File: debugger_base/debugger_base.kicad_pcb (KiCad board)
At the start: 4 copper layers, 57.4 x 50.8 mm, 62 parts, among them SW1 RESET, SW2 UART CHx LED enable switch, X1 USB-C Receptacle, X2 Channel A, X3 Channel B, X4 Channel C, X5 Channel D, Y1 12MHz

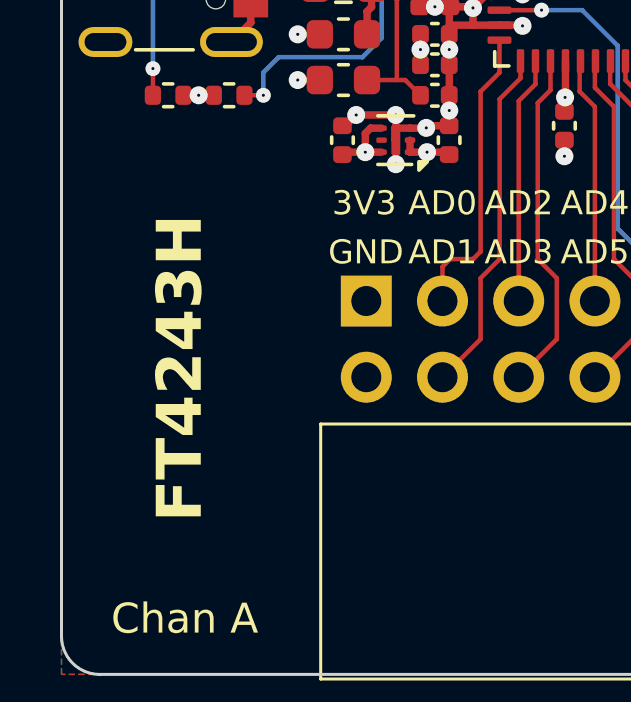
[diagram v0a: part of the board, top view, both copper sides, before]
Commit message: add version number to silkscreen
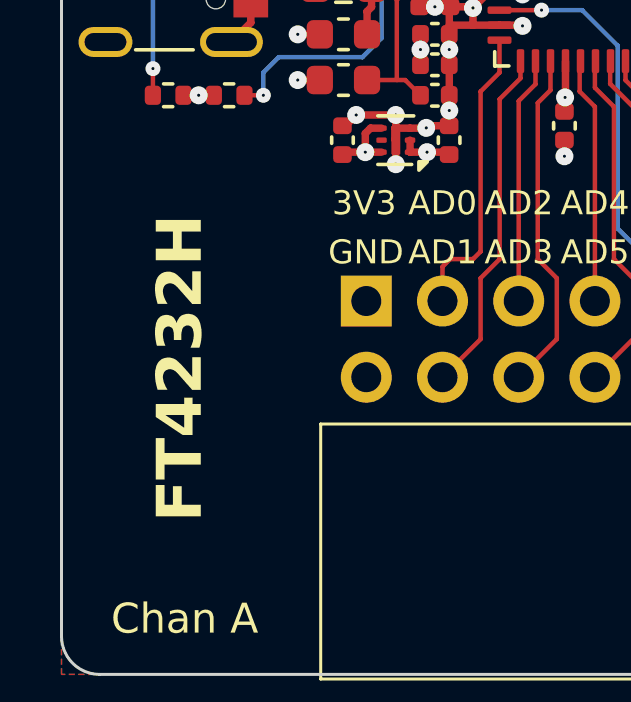
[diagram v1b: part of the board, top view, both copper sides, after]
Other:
- board text added: "FT4232H"
- board text added: "v0.1/04.24"
- board text removed: "FT4243H"
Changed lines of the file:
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@@
     )
     (stroke (width 0.15) (type solid)) (fill solid) (layer "User.1"))
+  (gr_text "v0.1/04.24" (at 147.066 82.931 90) (layer "B.SilkS")
+    (effects (font (size 1 1) (thickness 0.15)) (justify mirror))
+  )
   (gr_text "RX" (at 138.049 75.946 90) (layer "F.SilkS" knockout)
     (effects (font (size 1 1) (thickness 0.15)) (justify left bottom))
@@
     (effects (font (size 1 1) (thickness 0.15)) (justify left bottom))
   )
-  (gr_text "FT4243H" (at 101.346 102.87 90) (layer "F.SilkS")
+  (gr_text "FT4232H" (at 101.346 102.87 90) (layer "F.SilkS")
     (effects (font (size 1.5 1.5) (thickness 0.3) bold) (justify left bottom))
   )

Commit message: add design date
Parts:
- moved R6 4.97 mm to (143.9, 93.6), turned to -90 degrees
- moved R5 0.50 mm to (144.9, 101.6)
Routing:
- net /FT4232H/~{RESET}: track 51.4 -> 45.8 mm
- net /FT4232H/BDBUS0: track 51.3 -> 48.8 mm
- net /FT4232H/BDBUS1: track 51.9 -> 49.5 mm
- net /FT4232H/BDBUS2: track 44.9 -> 42.6 mm
- net /FT4232H/BDBUS3: track 46.1 -> 43.9 mm
- net /FT4232H/BDBUS4: track 39.7 -> 37.6 mm
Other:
- board text added: "3.3V @ 500mA"
- board text added: "v1.0/01.25"
- board text removed: "v0.1/04.24"

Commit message: decrease clearance of copper pours
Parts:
- V5: value 74HC595 -> DFN-16-1EP_2.5x2.5mm_P0.4mm_EP1.2x1.2mm
